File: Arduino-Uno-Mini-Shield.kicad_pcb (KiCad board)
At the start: 2 copper layers, 34.2 x 26.7 mm, 4 parts, among them J2 Conn_01x06, J3 Conn_01x08, J5 Conn_01x10

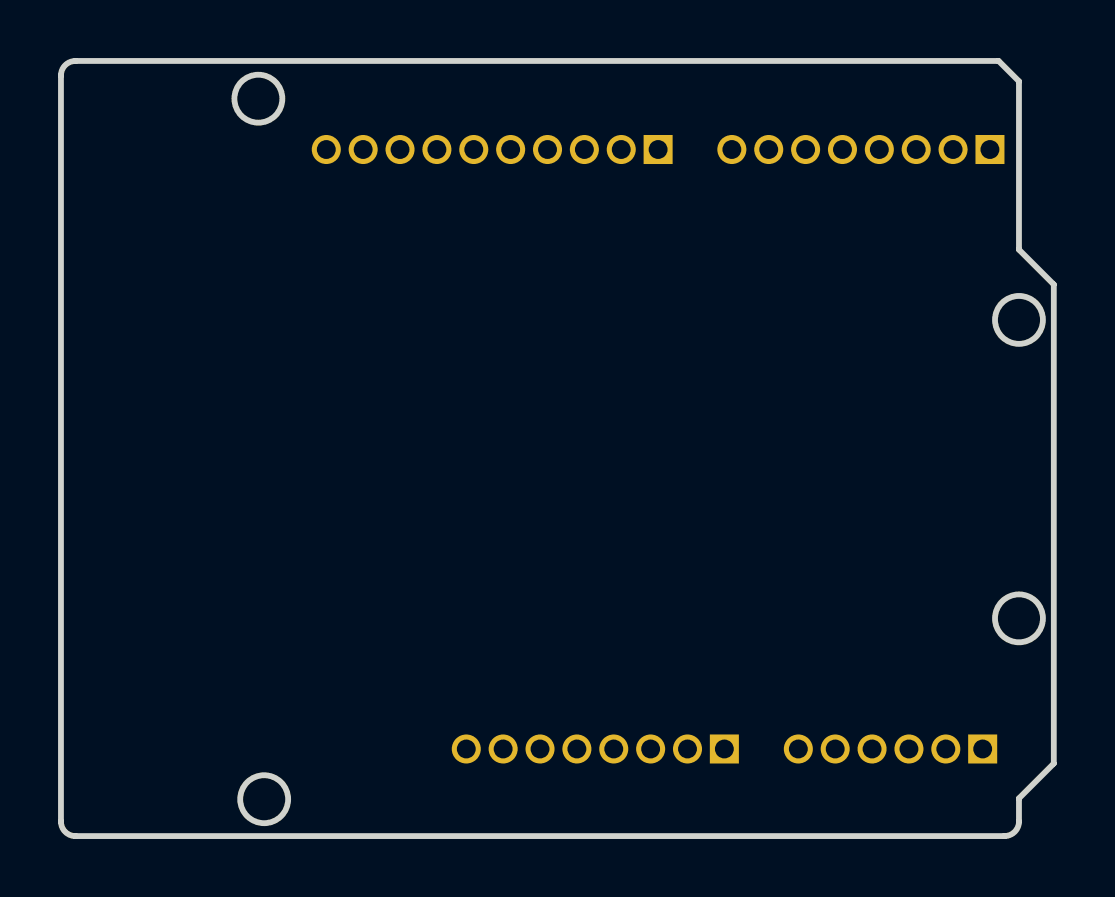
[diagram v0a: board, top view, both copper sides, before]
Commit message: final changes
added VIAS as mounting holes
added GND fill
added +5V connection
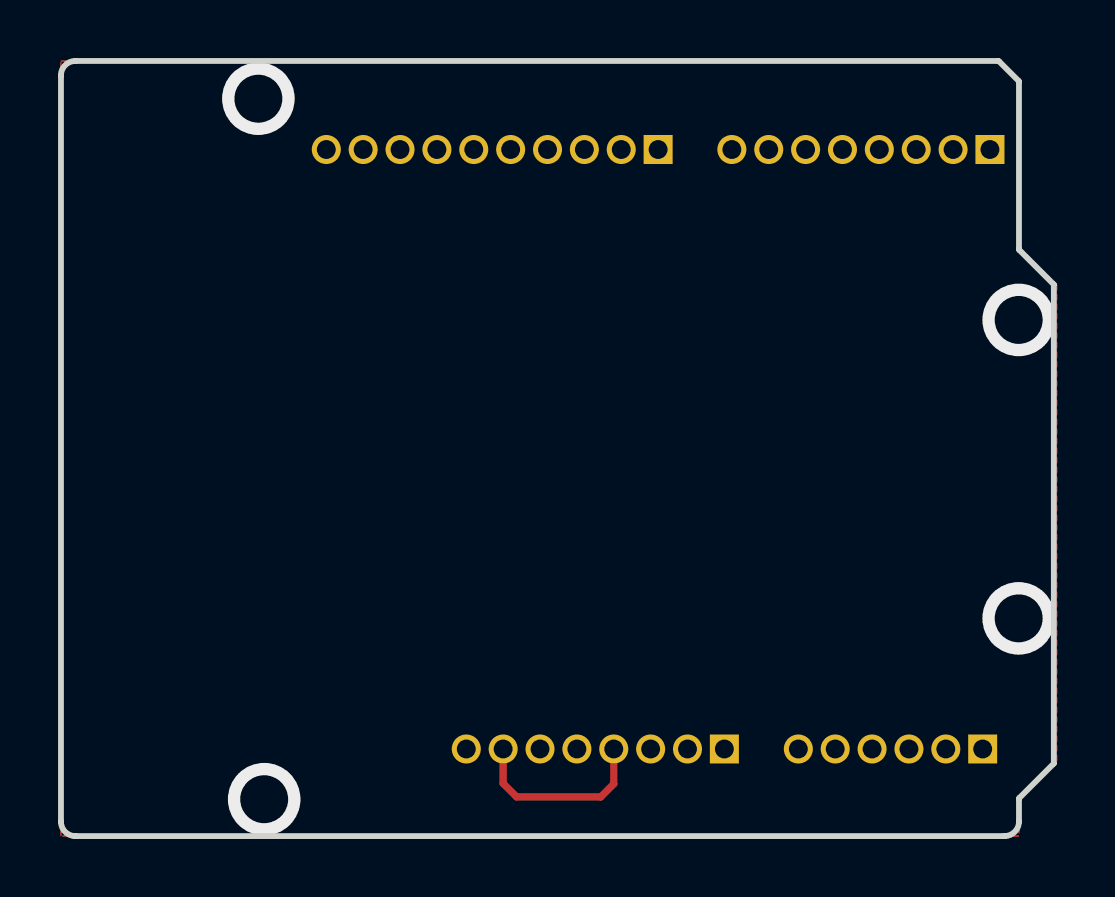
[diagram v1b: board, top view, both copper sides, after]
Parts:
- renumbered Je to J4
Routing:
- net /+5V: track 0.00 -> 6.58 mm
- net /GND: vias 0 -> 4
- added copper zone on B.Cu, net /GND
- added copper zone on F.Cu, net /GND
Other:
- outline, holes or cut-outs redrawn
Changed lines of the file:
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@@
     (48 "B.Fab" user)
     (49 "F.Fab" user)
-    (50 "User.1" user)
-    (51 "User.2" user)
-    (52 "User.3" user)
-    (53 "User.4" user)
-    (54 "User.5" user)
-    (55 "User.6" user)
-    (56 "User.7" user)
-    (57 "User.8" user)
-    (58 "User.9" user)
   )
   (setup
+    (stackup
+      (layer "F.SilkS" (type "Top Silk Screen"))
+      (layer "F.Paste" (type "Top Solder Paste"))
+      (layer "F.Mask" (type "Top Solder Mask") (thickness 0.01))
+      (layer "F.Cu" (type "copper") (thickness 0.035))
+      (layer "dielectric 1" (type "core") (thickness 1.51) (material "FR4") (epsilon_r 4.5) (loss_tangent 0.02))
+      (layer "B.Cu" (type "copper") (thickness 0.035))
+      (layer "B.Mask" (type "Bottom Solder Mask") (thickness 0.01))
+      (layer "B.Paste" (type "Bottom Solder Paste"))
+      (layer "B.SilkS" (type "Bottom Silk Screen"))
+      (copper_finish "ENIG")
+      (dielectric_constraints no)
+    )
     (pad_to_mask_clearance 0)
     (aux_axis_origin 78.994 85.372001)
@@
     (property "Sheetname" "")
     (attr through_hole)
-    (fp_text reference "Je" (at 0 1.695 90) (layer "B.SilkS")
+    (fp_text reference "J4" (at -2.099999 -4.45601 180) (layer "B.SilkS")
       (effects (font (size 1 1) (thickness 0.15)) (justify mirror))
     )
@@
     (property "Sheetname" "")
     (attr through_hole)
-    (fp_text reference "J2" (at 0 1.695 90) (layer "B.SilkS")
+    (fp_text reference "J2" (at -2.099999 -3.204001 180) (layer "B.SilkS")
       (effects (font (size 1 1) (thickness 0.15)) (justify mirror))
     )
@@
     (property "Sheetname" "")
     (attr through_hole)
-    (fp_text reference "J3" (at 0 1.695 90) (layer "B.SilkS")
+    (fp_text reference "J3" (at 1.999999 -4.454 180) (layer "B.SilkS")
       (effects (font (size 1 1) (thickness 0.15)) (justify mirror))
     )
@@
     (property "Sheetname" "")
     (attr through_hole)
-    (fp_text reference "J5" (at 0 1.695 90) (layer "B.SilkS")
+    (fp_text reference "J5" (at 1.949999 -6.374 180) (layer "B.SilkS")
       (effects (font (size 1 1) (thickness 0.15)) (justify mirror))
     )
@@
   (gr_line (start 111.998001 65.172001) (end 111.998001 59.372005) (layer "Edge.Cuts") (width 0.2))
   (gr_line (start 78.997998 59.172) (end 78.998001 84.872002) (layer "Edge.Cuts") (width 0.2))
-  (gr_circle (center 85.798 59.972001) (end 86.6235 59.972001) (layer "Edge.Cuts") (width 0.2) (fill none))
   (gr_line (start 111.998001 84.872002) (end 111.998001 84.072001) (layer "Edge.Cuts") (width 0.2))
   (gr_line (start 113.198001 82.872001) (end 113.198001 66.372001) (layer "Edge.Cuts") (width 0.2))
-  (gr_circle (center 111.998001 67.592001) (end 112.823501 67.592001) (layer "Edge.Cuts") (width 0.2) (fill none))
-  (gr_circle (center 85.998002 84.102001) (end 86.823502 84.102001) (layer "Edge.Cuts") (width 0.2) (fill none))
-  (gr_circle (center 111.998001 77.872001) (end 112.823501 77.872001) (layer "Edge.Cuts") (width 0.2) (fill none))
   (gr_arc (start 78.998001 59.172) (mid 79.144447 58.818447) (end 79.498 58.672001) (layer "Edge.Cuts") (width 0.2))
   (gr_arc (start 111.998001 84.872002) (mid 111.851554 85.225554) (end 111.498002 85.372001) (layer "Edge.Cuts") (width 0.2))
@@
   (gr_line (start 111.998001 84.072001) (end 113.198001 82.872001) (layer "Edge.Cuts") (width 0.2))
   (gr_line (start 79.498 58.672001) (end 111.298 58.672001) (layer "Edge.Cuts") (width 0.2))
+  (via (at 111.988001 77.872001) (size 2.5) (drill 1.651) (layers "F.Cu" "B.Cu") (free) (net 16))
+  (via (at 85.998002 84.102) (size 2.5) (drill 1.651) (layers "F.Cu" "B.Cu") (free) (net 16))
+  (via locked (at 85.798 59.972001) (size 2.5) (drill 1.651) (layers "F.Cu" "B.Cu") (free) (net 16))
+  (via (at 111.988001 67.592001) (size 2.5) (drill 1.651) (layers "F.Cu" "B.Cu") (free) (net 16))
+  (segment (start 97.594 84.022001) (end 98.04001 83.575991) (width 0.25) (layer "F.Cu") (net 17))
+  (segment (start 94.23001 82.372002) (end 94.23001 83.558011) (width 0.25) (layer "F.Cu") (net 17))
+  (segment (start 98.04001 83.575991) (end 98.04001 82.372002) (width 0.25) (layer "F.Cu") (net 17))
+  (segment (start 94.694 84.022001) (end 97.594 84.022001) (width 0.25) (layer "F.Cu") (net 17))
+  (segment (start 94.23001 83.558011) (end 94.694 84.022001) (width 0.25) (layer "F.Cu") (net 17))
+  (zone locked (net 16) (net_name "/GND") (layers F&B.Cu) (hatch edge 0.508)
+    (connect_pads (clearance 0.508))
+    (min_thickness 0.254) (filled_areas_thickness no)
+    (fill yes (thermal_gap 0.508) (thermal_bridge_width 0.508))
+    (polygon
+      (pts
+        (xy 112.044 59.422001)
+        (xy 112.044 65.122001)
+        (xy 113.294 66.372001)
+        (xy 113.294 82.772001)
+        (xy 111.994 84.072001)
+        (xy 111.994 85.372001)
+        (xy 78.994 85.372001)
+        (xy 78.994 58.672001)
+        (xy 111.294 58.672001)
+      )
+    )
+  )
 )
